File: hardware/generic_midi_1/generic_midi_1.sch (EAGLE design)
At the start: 20 parts, among them IC1 MEGA48/88/168-PU, IC2 RFM12

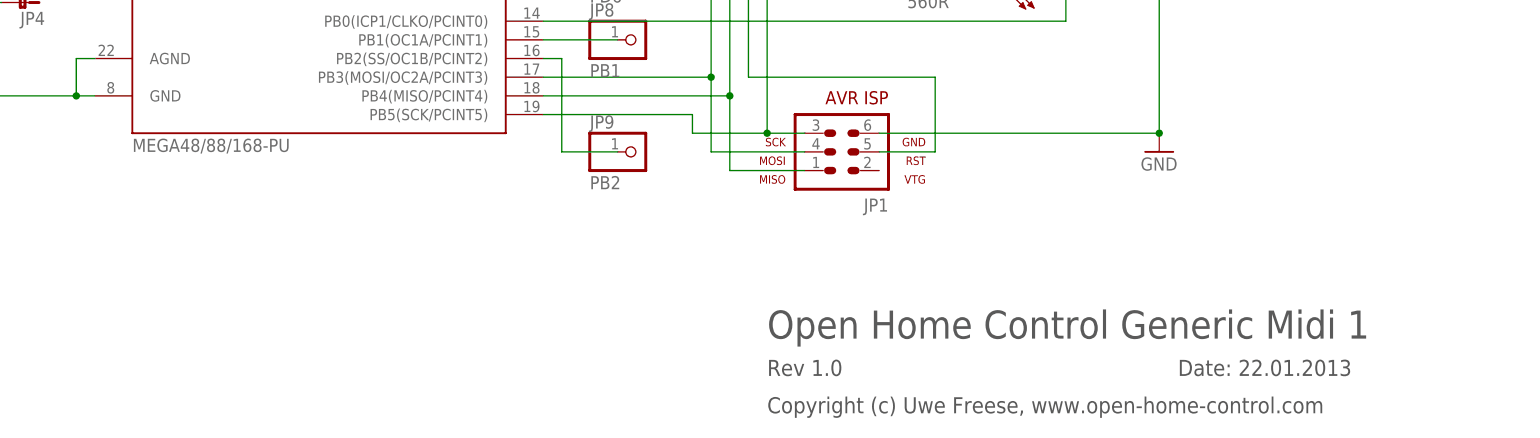
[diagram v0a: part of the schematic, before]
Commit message: Changed microcontroller name to MEGA168/328
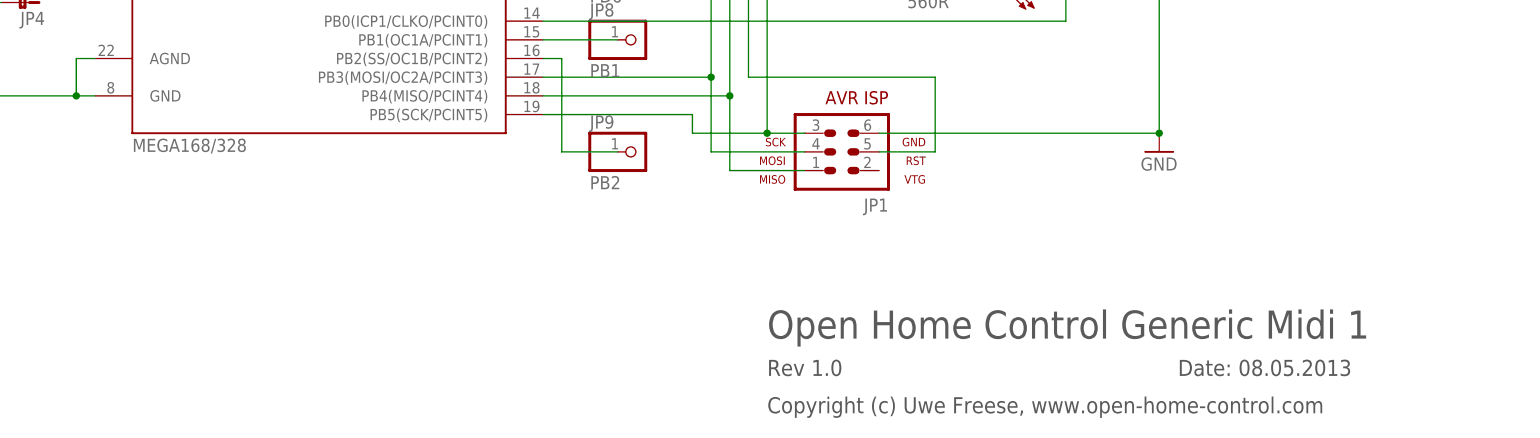
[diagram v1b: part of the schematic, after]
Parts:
- IC1: value MEGA48/88/168-PU -> MEGA168/328
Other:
- note added: "Date: 08.05.2013"
- note removed: "Date: 22.01.2013"
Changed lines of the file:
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@@
 <?xml version="1.0" encoding="utf-8"?>
 <!DOCTYPE eagle SYSTEM "eagle.dtd">
-<eagle version="6.2">
+<eagle version="6.4">
 <drawing>
 <settings>
@@
 <part name="IC2" library="hopeRF" deviceset="RFM12" device=""/>
 <part name="LED1" library="led" deviceset="LED" device="3MM" value="2mA"/>
-<part name="IC1" library="avr-5-4.16" deviceset="MEGA48/88/168-PU" device=""/>
+<part name="IC1" library="avr-5-4.16" deviceset="MEGA48/88/168-PU" device="" value="MEGA168/328"/>
 <part name="JP1" library="avr-5-4.16" deviceset="AVR-ISP-6" device=""/>
 <part name="P+1" library="supply1" deviceset="VCC" device=""/>
@@
 <frame x1="-60.96" y1="-63.5" x2="154.94" y2="88.9" columns="8" rows="5" layer="97"/>
 <text x="66.04" y="-43.18" size="3.81" layer="97">Open Home Control Generic Midi 1</text>
-<text x="121.92" y="-48.26" size="2.1844" layer="97">Date: 22.01.2013</text>
+<text x="121.92" y="-48.26" size="2.1844" layer="97">Date: 08.05.2013</text>
 <text x="66.04" y="-48.26" size="2.1844" layer="97">Rev 1.0</text>
 <text x="66.04" y="-53.34" size="2.1844" layer="97">Copyright (c) Uwe Freese, www.open-home-control.com</text>

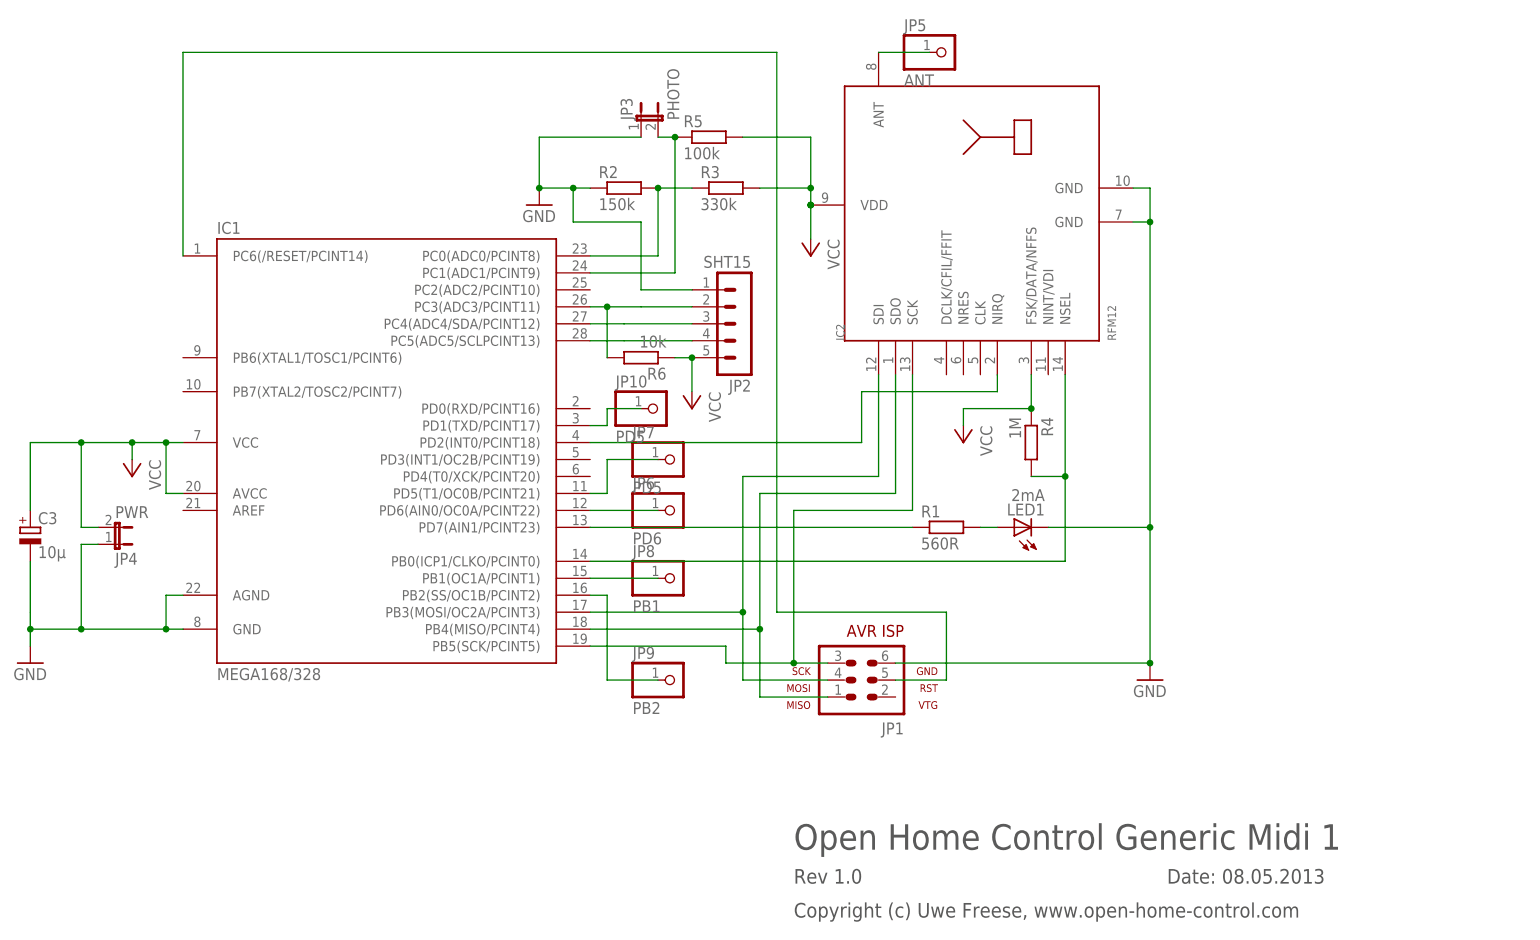
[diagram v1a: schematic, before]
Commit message: renames connectors, changed positions of labels, updated mask, placing and partlist
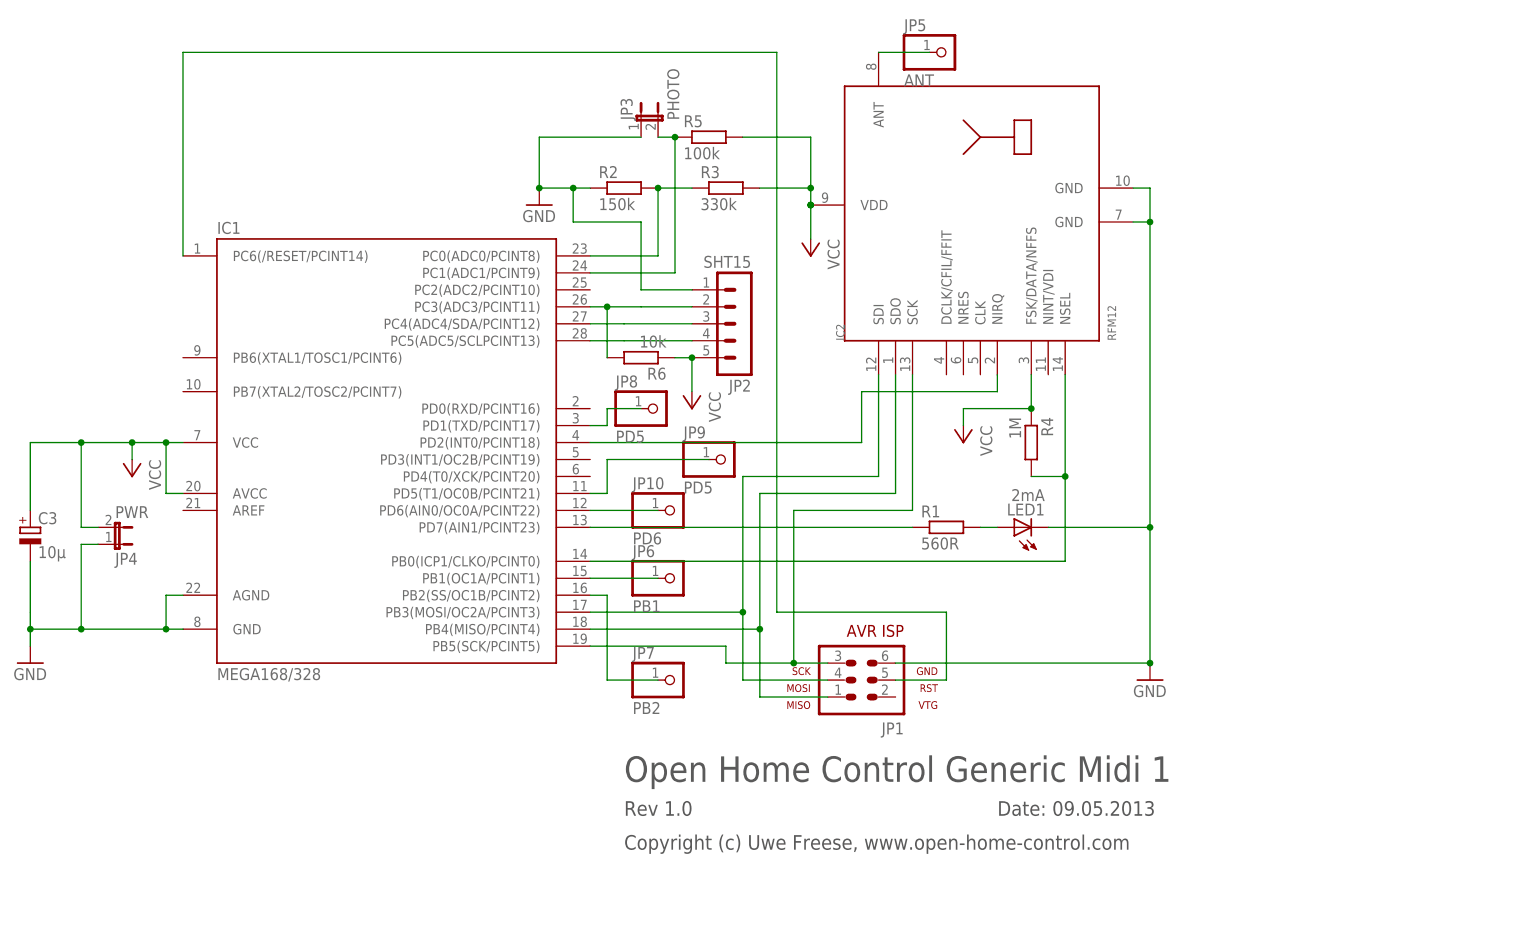
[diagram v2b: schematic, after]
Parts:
- JP10: value PD5 -> PD6
- JP6: value PD6 -> PB1
- JP7: value PD5 -> PB2
- JP8: value PB1 -> PD5
- JP9: value PB2 -> PD5
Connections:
- net N$14: now also JP9.1; no longer JP7.1
- net N$16: now also JP10.1; no longer JP6.1
- net N$17: now also JP6.1; no longer JP8.1
- net N$19: now also JP7.1; no longer JP9.1
- net N$20: now also JP8.1; no longer JP10.1
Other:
- note added: "Date: 09.05.2013"
- note removed: "Date: 08.05.2013"
- moved on the sheet: JP10, JP6, JP7, JP8, JP9
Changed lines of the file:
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@@
 <classes>
 <class number="0" name="default" width="0" drill="0">
+<clearance class="0" value="0.3048"/>
 </class>
 </classes>
@@
 <part name="JP4" library="jumper" deviceset="JP1E" device="" value="PWR"/>
 <part name="JP5" library="pinhead" deviceset="PINHD-1X1" device="" value="ANT"/>
-<part name="JP7" library="pinhead" deviceset="PINHD-1X1" device="" value="PD5"/>
-<part name="JP6" library="pinhead" deviceset="PINHD-1X1" device="" value="PD6"/>
-<part name="JP8" library="pinhead" deviceset="PINHD-1X1" device="" value="PB1"/>
-<part name="JP9" library="pinhead" deviceset="PINHD-1X1" device="" value="PB2"/>
+<part name="JP9" library="pinhead" deviceset="PINHD-1X1" device="" value="PD5"/>
+<part name="JP10" library="pinhead" deviceset="PINHD-1X1" device="" value="PD6"/>
+<part name="JP6" library="pinhead" deviceset="PINHD-1X1" device="" value="PB1"/>
+<part name="JP7" library="pinhead" deviceset="PINHD-1X1" device="" value="PB2"/>
 <part name="R6" library="rcl" deviceset="R-EU_" device="0207/7" value="10k"/>
-<part name="JP10" library="pinhead" deviceset="PINHD-1X1" device="" value="PD5"/>
+<part name="JP8" library="pinhead" deviceset="PINHD-1X1" device="" value="PD5"/>
 </parts>
 <sheets>
 <sheet>
 <plain>
-<frame x1="-60.96" y1="-63.5" x2="154.94" y2="88.9" columns="8" rows="5" layer="97"/>
-<text x="66.04" y="-43.18" size="3.81" layer="97">Open Home Control Generic Midi 1</text>
-<text x="121.92" y="-48.26" size="2.1844" layer="97">Date: 08.05.2013</text>
-<text x="66.04" y="-48.26" size="2.1844" layer="97">Rev 1.0</text>
-<text x="66.04" y="-53.34" size="2.1844" layer="97">Copyright (c) Uwe Freese, www.open-home-control.com</text>
+<frame x1="-60.96" y1="-53.34" x2="132.08" y2="88.9" columns="8" rows="5" layer="97"/>
+<text x="40.64" y="-33.02" size="3.81" layer="97">Open Home Control Generic Midi 1</text>
+<text x="96.52" y="-38.1" size="2.1844" layer="97">Date: 09.05.2013</text>
+<text x="40.64" y="-38.1" size="2.1844" layer="97">Rev 1.0</text>
+<text x="40.64" y="-43.18" size="2.1844" layer="97">Copyright (c) Uwe Freese, www.open-home-control.com</text>
 </plain>
 <instances>
@@
 <instance part="JP4" gate="A" x="-35.56" y="2.54" rot="MR90"/>
 <instance part="JP5" gate="G$1" x="88.9" y="76.2"/>
-<instance part="JP7" gate="G$1" x="48.26" y="15.24"/>
-<instance part="JP6" gate="G$1" x="48.26" y="7.62"/>
-<instance part="JP8" gate="G$1" x="48.26" y="-2.54"/>
-<instance part="JP9" gate="G$1" x="48.26" y="-17.78"/>
+<instance part="JP9" gate="G$1" x="55.88" y="15.24"/>
+<instance part="JP10" gate="G$1" x="48.26" y="7.62"/>
+<instance part="JP6" gate="G$1" x="48.26" y="-2.54"/>
+<instance part="JP7" gate="G$1" x="48.26" y="-17.78"/>
 <instance part="R6" gate="G$1" x="43.18" y="30.48" rot="R180"/>
-<instance part="JP10" gate="G$1" x="45.72" y="22.86"/>
+<instance part="JP8" gate="G$1" x="45.72" y="22.86"/>
 </instances>
 <busses>
@@
 <wire x1="35.56" y1="10.16" x2="38.1" y2="10.16" width="0.1524" layer="91"/>
 <wire x1="38.1" y1="10.16" x2="38.1" y2="15.24" width="0.1524" layer="91"/>
-<pinref part="JP7" gate="G$1" pin="1"/>
-<wire x1="38.1" y1="15.24" x2="45.72" y2="15.24" width="0.1524" layer="91"/>
+<pinref part="JP9" gate="G$1" pin="1"/>
+<wire x1="38.1" y1="15.24" x2="53.34" y2="15.24" width="0.1524" layer="91"/>
 </segment>
 </net>
@@
 <segment>
 <pinref part="IC1" gate="1" pin="PD6(AIN0/OC0A/PCINT22)"/>
+<pinref part="JP10" gate="G$1" pin="1"/>
+<wire x1="35.56" y1="7.62" x2="45.72" y2="7.62" width="0.1524" layer="91"/>
+</segment>
+</net>
+<net name="N$17" class="0">
+<segment>
+<pinref part="IC1" gate="1" pin="PB1(OC1A/PCINT1)"/>
 <pinref part="JP6" gate="G$1" pin="1"/>
-<wire x1="35.56" y1="7.62" x2="45.72" y2="7.62" width="0.1524" layer="91"/>
-</segment>
-</net>
-<net name="N$17" class="0">
-<segment>
-<pinref part="IC1" gate="1" pin="PB1(OC1A/PCINT1)"/>
-<pinref part="JP8" gate="G$1" pin="1"/>
 <wire x1="35.56" y1="-2.54" x2="45.72" y2="-2.54" width="0.1524" layer="91"/>
 </segment>
@@
 <wire x1="35.56" y1="-5.08" x2="38.1" y2="-5.08" width="0.1524" layer="91"/>
 <wire x1="38.1" y1="-5.08" x2="38.1" y2="-17.78" width="0.1524" layer="91"/>
-<pinref part="JP9" gate="G$1" pin="1"/>
+<pinref part="JP7" gate="G$1" pin="1"/>
 <wire x1="38.1" y1="-17.78" x2="45.72" y2="-17.78" width="0.1524" layer="91"/>
 </segment>
@@
 <wire x1="35.56" y1="20.32" x2="38.1" y2="20.32" width="0.1524" layer="91"/>
 <wire x1="38.1" y1="20.32" x2="38.1" y2="22.86" width="0.1524" layer="91"/>
-<pinref part="JP10" gate="G$1" pin="1"/>
+<pinref part="JP8" gate="G$1" pin="1"/>
 <wire x1="38.1" y1="22.86" x2="43.18" y2="22.86" width="0.1524" layer="91"/>
 </segment>
